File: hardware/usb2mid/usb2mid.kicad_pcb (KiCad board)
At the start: 4 copper layers, 40 x 12 mm, 27 parts, among them J1 USB_C_Receptacle_USB2.0_16P, J2 AudioJack3, U1 STM32G0C1KCUx, U2 USBLC6-2SC6, U3 BU33SD5WG-TR

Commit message: minor corrections + gerber
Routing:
- net +3.3V: track 23.2 -> 23.7 mm
- net GND: track 12.3 -> 12.8 mm, vias 18 -> 37
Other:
- outline, holes or cut-outs redrawn
- board text added: "+3.3V"
- board text added: "GND"
- board text added: "JLCJLCJLCJLC"
- board text added: "NRST"
- board text added: "RX"
- board text added: "SWDCLK"
- board text added: "SWDIO"
- board text added: "TX"
- board text added: "WITNS - USB2MID L.FIACK 29/02/2024"

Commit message: changed USB-C footprint
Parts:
- J1: footprint Connector_USB:USB_C_Receptacle_HRO_TYPE-C-31-M-12 -> Connector_USB:USB_C_Receptacle_GCT_USB4105-xx-A_16P_TopMnt_Horizontal
- U1: value STM32G0C1KCUx -> STM32G0C1KCU6
- moved J1 0.30 mm to (25.3, 50.0)
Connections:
- U1 pad 31: /MIDI_RX -> unconnected-(U1-PB7-Pad31)

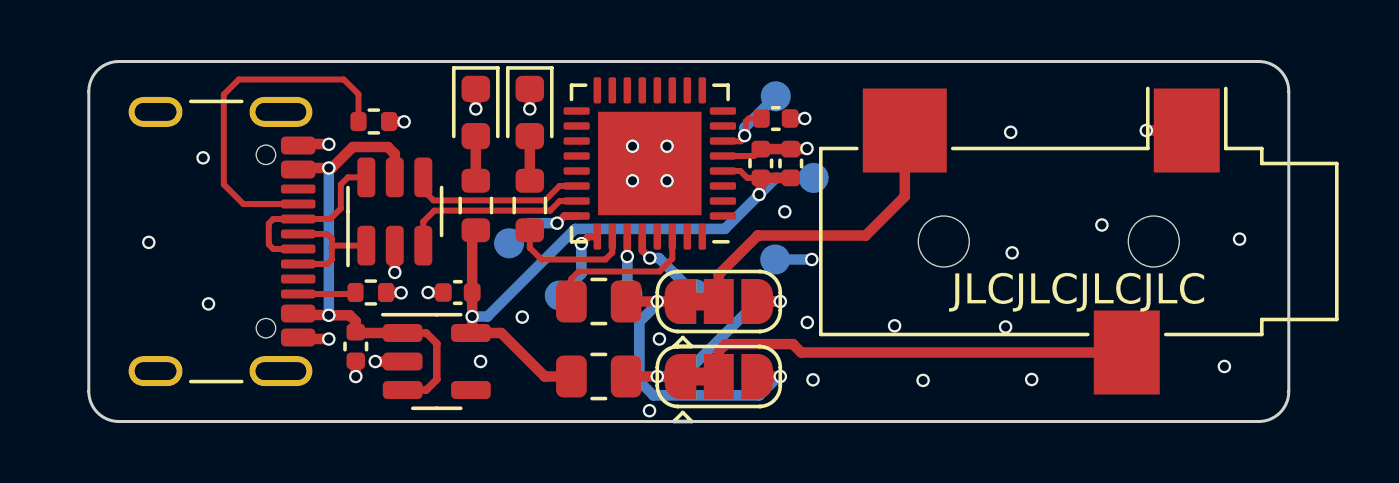
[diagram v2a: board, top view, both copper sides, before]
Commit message: oops USB ESD!!
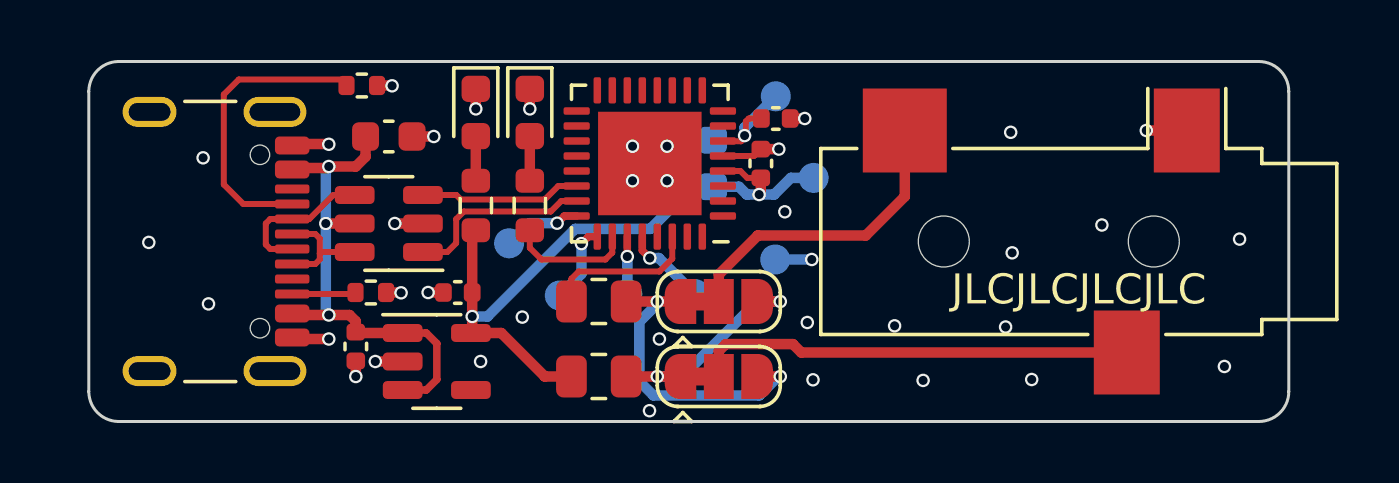
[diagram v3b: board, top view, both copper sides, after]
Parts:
- added C7: 10uF, Capacitor_SMD:C_0603_1608Metric, F.Cu at (32.0, 46.5)
- C2: footprint Capacitor_SMD:C_0402_1005Metric -> Capacitor_SMD:C_0603_1608Metric; moved to B.Cu
- moved C2 2.60 mm to (42.8, 47.4)
- moved R1 1.26 mm to (31.1, 44.8)
- moved U2 0.45 mm to (32.0, 49.4), turned to 180 degrees
- moved J1 0.20 mm to (25.1, 50.0)
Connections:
- U2 pad 1: /D+ -> /USB_DP
- U2 pad 3: /USB_DP -> /USB_DM
- U2 pad 4: /USB_DM -> /D-
- U2 pad 6: /D- -> /D+
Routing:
- net /CC1: track 11.6 -> 10.0 mm
- net GND: track 12.8 -> 14.3 mm, vias 37 -> 38
- net /D-: track 6.16 -> 5.00 mm
- net +3.3V: track 23.7 -> 22.9 mm
- net /USB_DM: track 5.88 -> 5.37 mm
- net VBUS: track 16.9 -> 16.6 mm, vias 2 -> 3

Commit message: minor corrections to PCB
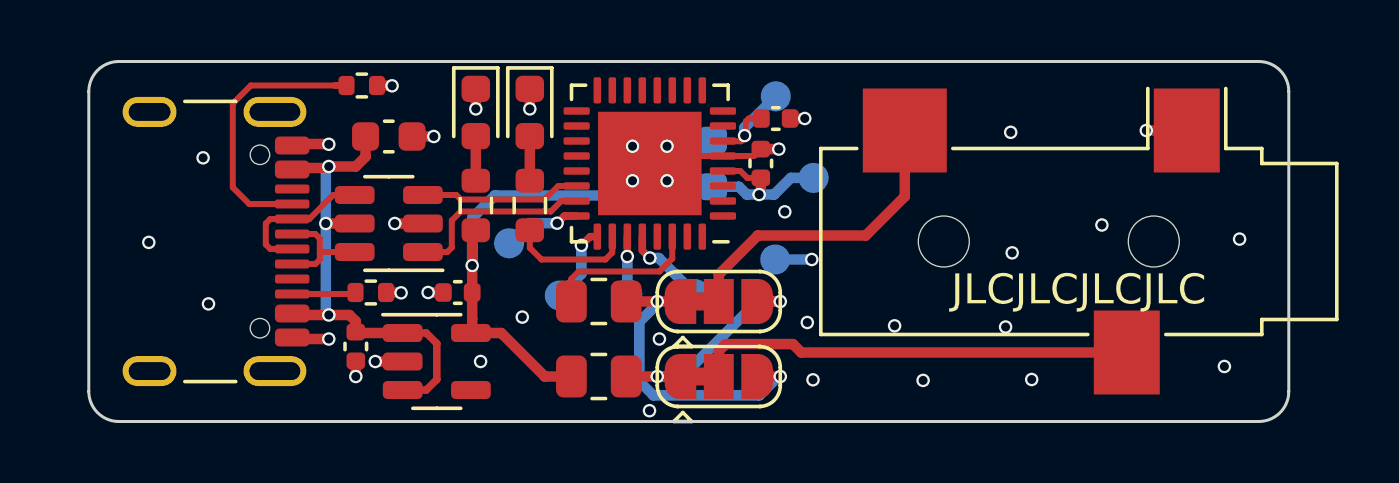
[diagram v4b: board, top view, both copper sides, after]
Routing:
- net GND: track 14.3 -> 16.9 mm
- net /CC1: track 10.0 -> 9.41 mm
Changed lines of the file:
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@@
 	)
 	(via
-		(at 34.78 52.5)
+		(at 34.78 50.8)
 		(size 0.45)
 		(drill 0.3)
@@
 	)
 	(segment
-		(start 34.78 52.5)
-		(end 35.29 52.5)
+		(start 35.535 48.465)
+		(end 41.835 48.465)
 		(width 0.35)
 		(layer "B.Cu")
@@
 	)
 	(segment
-		(start 42.9 48.175)
+		(start 43.675 48.175)
+		(end 43.935 48.435)
+		(width 0.35)
+		(layer "B.Cu")
+		(net 1)
+	)
+	(segment
+		(start 34.78 49.22)
+		(end 35.535 48.465)
+		(width 0.35)
+		(layer "B.Cu")
+		(net 1)
+	)
+	(segment
+		(start 41.835 48.465)
+		(end 42.125 48.175)
+		(width 0.35)
+		(layer "B.Cu")
+		(net 1)
+	)
+	(segment
+		(start 34.78 50.8)
+		(end 34.78 49.22)
+		(width 0.35)
+		(layer "B.Cu")
+		(net 1)
+	)
+	(segment
+		(start 42.125 48.175)
 		(end 43.675 48.175)
 		(width 0.35)
@@
 	)
 	(segment
-		(start 42.125 48.175)
-		(end 42.9 48.175)
+		(start 44.345 48.435)
+		(end 44.845 48.435)
 		(width 0.35)
 		(layer "B.Cu")
@@
 	)
 	(segment
-		(start 40.72 49.58)
-		(end 42.125 48.175)
-		(width 0.35)
-		(layer "B.Cu")
-		(net 1)
-	)
-	(segment
-		(start 38.21 49.58)
-		(end 40.72 49.58)
-		(width 0.35)
-		(layer "B.Cu")
-		(net 1)
-	)
-	(segment
-		(start 35.29 52.5)
-		(end 38.21 49.58)
-		(width 0.35)
-		(layer "B.Cu")
-		(net 1)
-	)
-	(segment
-		(start 43.675 48.175)
-		(end 43.935 48.435)
-		(width 0.35)
-		(layer "B.Cu")
-		(net 1)
-	)
-	(segment
-		(start 44.345 48.435)
-		(end 44.845 48.435)
-		(width 0.35)
-		(layer "B.Cu")
-		(net 1)
+		(start 43.1375 47.15)
+		(end 40.95 47.15)
+		(width 0.2)
+		(layer "F.Cu")
+		(net 2)
 	)
 	(segment
@@
 	)
 	(segment
+		(start 40.95 47.15)
+		(end 40.7 47.4)
+		(width 0.2)
+		(layer "F.Cu")
+		(net 2)
+	)
+	(segment
 		(start 32.1 44.8)
 		(end 31.61 44.8)
@@
 	)
 	(segment
+		(start 37.2 48.6)
+		(end 34.4 48.6)
+		(width 0.2)
+		(layer "F.Cu")
+		(net 22)
+	)
+	(segment
 		(start 38.2625 48.15)
 		(end 37.65 48.15)
@@
 	)
 	(segment
-		(start 37.2 48.6)
-		(end 34.4 48.6)
-		(width 0.2)
-		(layer "F.Cu")
-		(net 22)
-	)
-	(segment
 		(start 34.4 48.6)
 		(end 34.25 48.45)
@@
 	)
 	(segment
-		(start 34.5 49)
-		(end 34.245 49.255)
+		(start 34.4 49)
+		(end 34.1 49.3)
 		(width 0.2)
 		(layer "F.Cu")
@@
 	)
 	(segment
-		(start 34.245 49.255)
-		(end 34.245 50.055)
+		(start 33.95 50.35)
+		(end 33.1375 50.35)
 		(width 0.2)
 		(layer "F.Cu")
@@
 	)
 	(segment
-		(start 34.245 50.055)
+		(start 37.4 49)
+		(end 34.4 49)
+		(width 0.2)
+		(layer "F.Cu")
+		(net 23)
+	)
+	(segment
+		(start 37.75 48.65)
+		(end 37.4 49)
+		(width 0.2)
+		(layer "F.Cu")
+		(net 23)
+	)
+	(segment
+		(start 34.1 50.2)
 		(end 33.95 50.35)
 		(width 0.2)
@@
 	)
 	(segment
-		(start 37.75 48.65)
-		(end 37.4 49)
-		(width 0.2)
-		(layer "F.Cu")
-		(net 23)
-	)
-	(segment
-		(start 37.4 49)
-		(end 34.5 49)
-		(width 0.2)
-		(layer "F.Cu")
-		(net 23)
-	)
-	(segment
-		(start 33.95 50.35)
-		(end 33.1375 50.35)
+		(start 34.1 49.3)
+		(end 34.1 50.2)
 		(width 0.2)
 		(layer "F.Cu")
@@
 	)
 	(segment
-		(start 38.95 49.8375)
-		(end 38.6525 49.8375)
+		(start 38.7125 49.8375)
+		(end 38.95 49.8375)
 		(width 0.25)
 		(layer "F.Cu")
@@
 	)
 	(segment
-		(start 38.6525 49.8375)
-		(end 38.42 50.07)
+		(start 38.42 50.13)
+		(end 38.7125 49.8375)
 		(width 0.25)
 		(layer "F.Cu")
@@
 	)
 	(via
-		(at 38.42 50.07)
+		(at 38.42 50.13)
 		(size 0.45)
 		(drill 0.3)
@@
 	)
 	(segment
-		(start 38.42 50.07)
+		(start 38.42 50.13)
 		(end 38.42 51.08)
 		(width 0.35)
@@
 	)
 	(segment
+		(start 26.8 48.2)
+		(end 26.8 45.4)
+		(width 0.2)
+		(layer "F.Cu")
+		(net 36)
+	)
+	(segment
+		(start 27.4 44.8)
+		(end 30.2 44.8)
+		(width 0.2)
+		(layer "F.Cu")
+		(net 36)
+	)
+	(segment
+		(start 26.8 45.4)
+		(end 27.4 44.8)
+		(width 0.2)
+		(layer "F.Cu")
+		(net 36)
+	)
+	(segment
+		(start 30.2 44.8)
+		(end 30.3 44.8)
+		(width 0.2)
+		(layer "F.Cu")
+		(net 36)
+	)
+	(segment
+		(start 30.2 44.8)
+		(end 30.59 44.8)
+		(width 0.2)
+		(layer "F.Cu")
+		(net 36)
+	)
+	(segment
+		(start 27.35 48.75)
+		(end 26.8 48.2)
+		(width 0.2)
+		(layer "F.Cu")
+		(net 36)
+	)
+	(segment
 		(start 29.045 48.75)
-		(end 27.15 48.75)
-		(width 0.2)
-		(layer "F.Cu")
-		(net 36)
-	)
-	(segment
-		(start 27 44.6)
-		(end 30.5 44.6)
-		(width 0.2)
-		(layer "F.Cu")
-		(net 36)
-	)
-	(segment
-		(start 26.5 45.1)
-		(end 27 44.6)
-		(width 0.2)
-		(layer "F.Cu")
-		(net 36)
-	)
-	(segment
-		(start 27.15 48.75)
-		(end 26.5 48.1)
-		(width 0.2)
-		(layer "F.Cu")
-		(net 36)
-	)
-	(segment
-		(start 26.5 48.1)
-		(end 26.5 45.1)
-		(width 0.2)
-		(layer "F.Cu")
+		(end 27.35 48.75)
+		(width 0.2)
+		(layer "F.Cu")
